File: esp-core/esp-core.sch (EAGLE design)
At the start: 6 parts

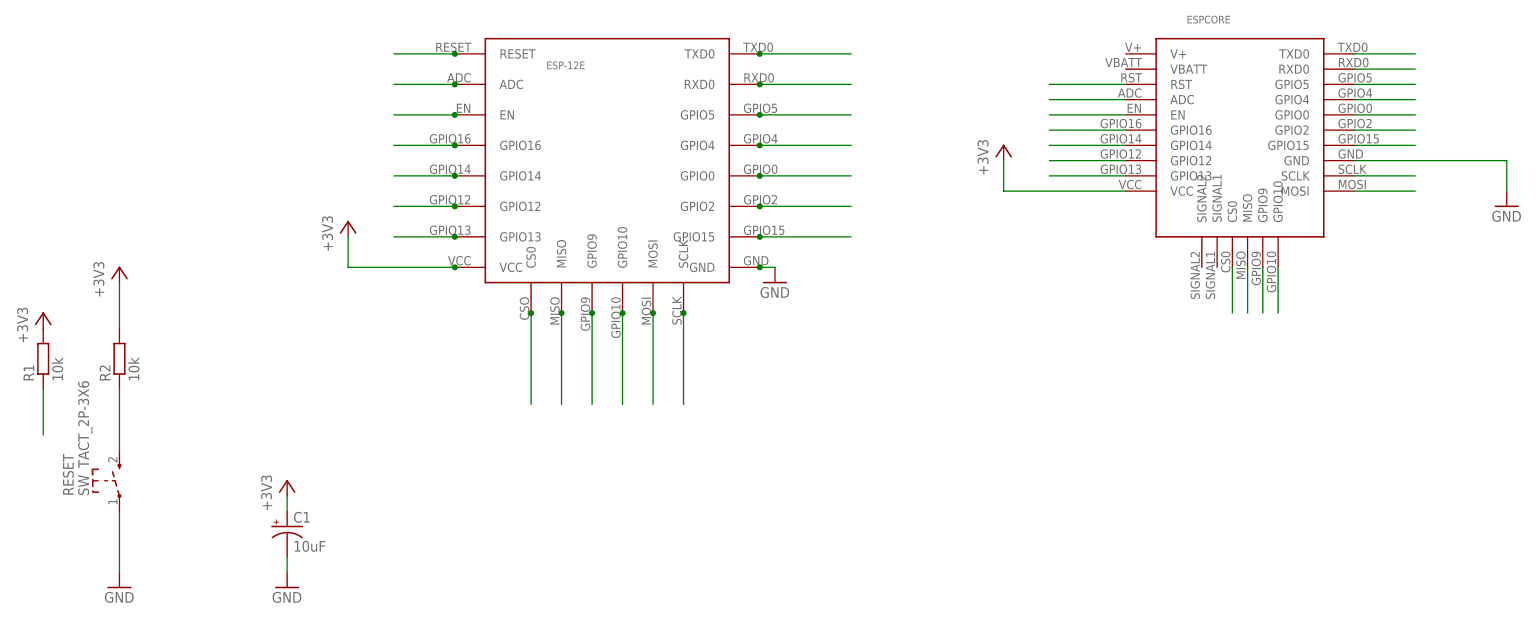
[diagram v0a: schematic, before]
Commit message: Add pull-up and down resistors to 'special' pins - GPIO0 and GPIO15
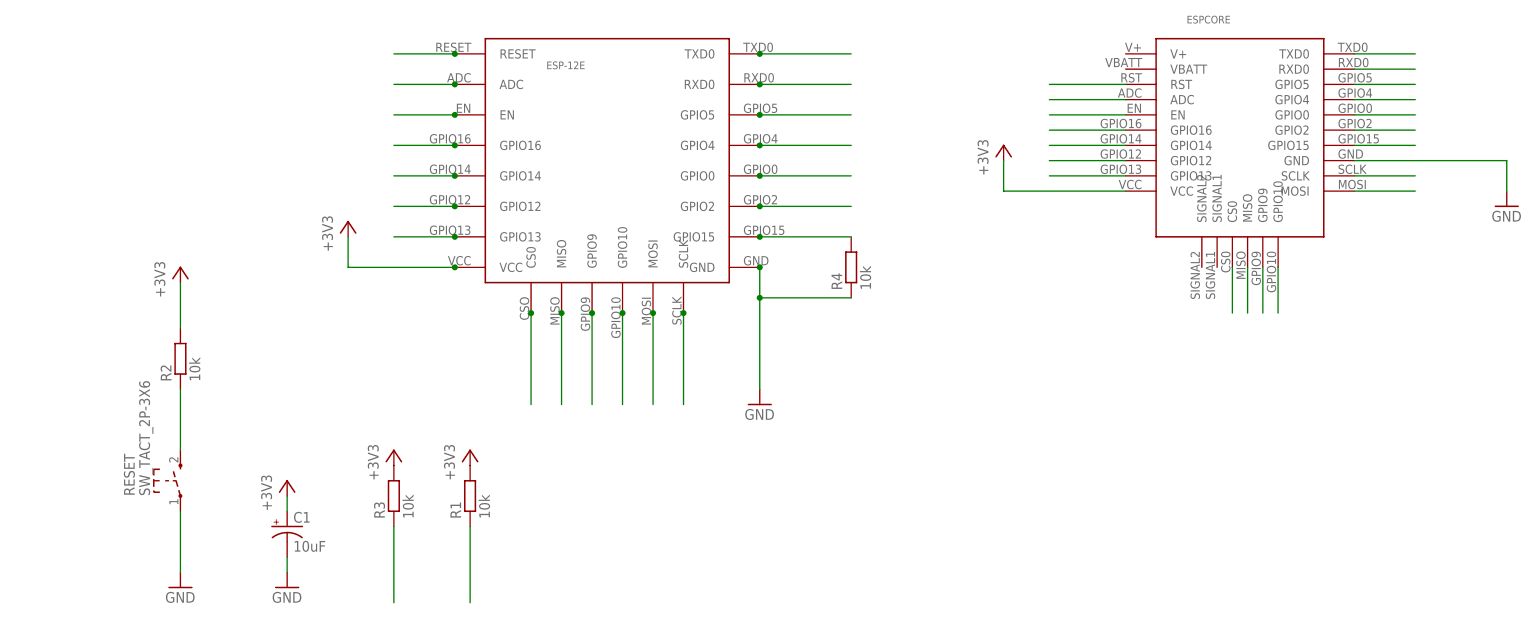
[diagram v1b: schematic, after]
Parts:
- added R3, R4: 10k, dp_devices:RESISTOR-1206
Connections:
- net +3V3: now also R3.2
- net GND: now also R4.1
- net GPIO0: now also R3.1
- net GPIO15: now also R4.2
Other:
- moved on the sheet: R1, R2, RESET
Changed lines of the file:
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@@
 <part name="ESPCORE" library="ESPstack" deviceset="ESP-BOARD" device=""/>
 <part name="ESP-12E" library="ESPstack" deviceset="ESP-12E" device=""/>
+<part name="R3" library="dp_devices" deviceset="RESISTOR" device="-1206" value="10k"/>
+<part name="R4" library="dp_devices" deviceset="RESISTOR" device="-1206" value="10k"/>
+<part name="+3V6" library="supply1" deviceset="+3V3" device=""/>
 </parts>
 <sheets>
@@
 </plain>
 <instances>
-<instance part="R1" gate="G$1" x="-144.78" y="-10.16" rot="R90"/>
-<instance part="R2" gate="G$1" x="-132.08" y="-10.16" rot="R90"/>
-<instance part="RESET" gate="SW" x="-132.08" y="-30.48" rot="R90"/>
+<instance part="R1" gate="G$1" x="-73.66" y="-33.02" rot="R90"/>
+<instance part="R2" gate="G$1" x="-121.92" y="-10.16" rot="R90"/>
+<instance part="RESET" gate="SW" x="-121.92" y="-30.48" rot="R90"/>
 <instance part="+3V1" gate="G$1" x="15.24" y="25.4"/>
-<instance part="+3V2" gate="G$1" x="-144.78" y="-2.54"/>
-<instance part="+3V3" gate="G$1" x="-132.08" y="5.08"/>
+<instance part="+3V2" gate="G$1" x="-73.66" y="-25.4"/>
+<instance part="+3V3" gate="G$1" x="-121.92" y="5.08"/>
 <instance part="+3V4" gate="G$1" x="-93.98" y="12.7"/>
 <instance part="GND1" gate="1" x="99.06" y="15.24"/>
-<instance part="GND3" gate="1" x="-22.86" y="2.54"/>
-<instance part="GND4" gate="1" x="-132.08" y="-48.26"/>
+<instance part="GND3" gate="1" x="-25.4" y="-17.78"/>
+<instance part="GND4" gate="1" x="-121.92" y="-48.26"/>
 <instance part="+3V5" gate="G$1" x="-104.14" y="-30.48"/>
 <instance part="GND5" gate="1" x="-104.14" y="-48.26"/>
@@
 <instance part="ESPCORE" gate="G$1" x="53.34" y="27.94"/>
 <instance part="ESP-12E" gate="G$1" x="-48.26" y="17.78"/>
+<instance part="R3" gate="G$1" x="-86.36" y="-33.02" rot="R90"/>
+<instance part="R4" gate="G$1" x="-10.16" y="5.08" rot="R90"/>
+<instance part="+3V6" gate="G$1" x="-86.36" y="-25.4"/>
 </instances>
 <busses>
@@
 <wire x1="73.66" y1="30.48" x2="83.82" y2="30.48" width="0.1524" layer="91"/>
 </segment>
+<segment>
+<pinref part="R3" gate="G$1" pin="1"/>
+<wire x1="-86.36" y1="-38.1" x2="-86.36" y2="-50.8" width="0.1524" layer="91"/>
+</segment>
 </net>
 <net name="GPIO2" class="0">
@@
 <pinref part="ESP-12E" gate="G$1" pin="GPIO15"/>
 <junction x="-25.4" y="10.16"/>
+<pinref part="R4" gate="G$1" pin="2"/>
 </segment>
 <segment>
@@
 <pinref part="GND4" gate="1" pin="GND"/>
 <pinref part="RESET" gate="SW" pin="1"/>
-<wire x1="-132.08" y1="-35.56" x2="-132.08" y2="-45.72" width="0.1524" layer="91"/>
-</segment>
-<segment>
-<wire x1="-25.4" y1="5.08" x2="-22.86" y2="5.08" width="0.1524" layer="91"/>
+<wire x1="-121.92" y1="-35.56" x2="-121.92" y2="-45.72" width="0.1524" layer="91"/>
+</segment>
+<segment>
+<wire x1="-25.4" y1="5.08" x2="-25.4" y2="0" width="0.1524" layer="91"/>
 <pinref part="GND3" gate="1" pin="GND"/>
 <pinref part="ESP-12E" gate="G$1" pin="GND"/>
 <junction x="-25.4" y="5.08"/>
+<pinref part="R4" gate="G$1" pin="1"/>
+<wire x1="-25.4" y1="0" x2="-25.4" y2="-15.24" width="0.1524" layer="91"/>
+<wire x1="-10.16" y1="0" x2="-25.4" y2="0" width="0.1524" layer="91"/>
+<junction x="-25.4" y="0"/>
 </segment>
 <segment>
@@
 <pinref part="+3V3" gate="G$1" pin="+3V3"/>
 <pinref part="R2" gate="G$1" pin="2"/>
-<wire x1="-132.08" y1="2.54" x2="-132.08" y2="-5.08" width="0.1524" layer="91"/>
+<wire x1="-121.92" y1="2.54" x2="-121.92" y2="-5.08" width="0.1524" layer="91"/>
 </segment>
 <segment>
@@
 <wire x1="-104.14" y1="-35.56" x2="-104.14" y2="-33.02" width="0.1524" layer="91"/>
 </segment>
+<segment>
+<pinref part="R3" gate="G$1" pin="2"/>
+<pinref part="+3V6" gate="G$1" pin="+3V3"/>
+</segment>
 </net>
 <net name="RESET" class="0">
@@
 <pinref part="RESET" gate="SW" pin="3"/>
 <pinref part="R2" gate="G$1" pin="1"/>
-<wire x1="-132.08" y1="-25.4" x2="-132.08" y2="-15.24" width="0.1524" layer="91"/>
+<wire x1="-121.92" y1="-25.4" x2="-121.92" y2="-15.24" width="0.1524" layer="91"/>
 </segment>
 <segment>
@@
 <segment>
 <pinref part="R1" gate="G$1" pin="1"/>
-<wire x1="-144.78" y1="-22.86" x2="-144.78" y2="-15.24" width="0.1524" layer="91"/>
-</segment>
-<segment>
+<wire x1="-73.66" y1="-50.8" x2="-73.66" y2="-38.1" width="0.1524" layer="91"/>
+</segment>
+<segment>

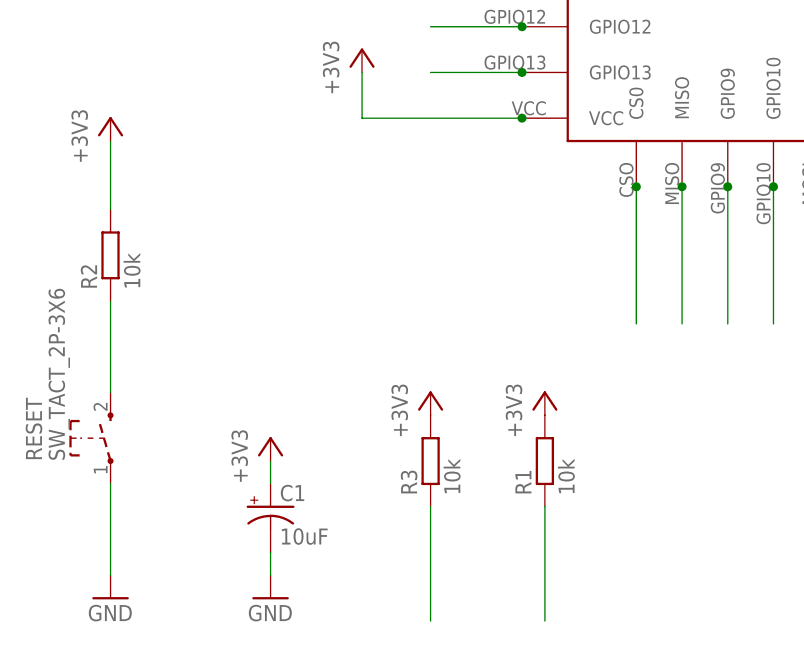
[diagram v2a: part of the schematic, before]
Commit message: Fix button on board
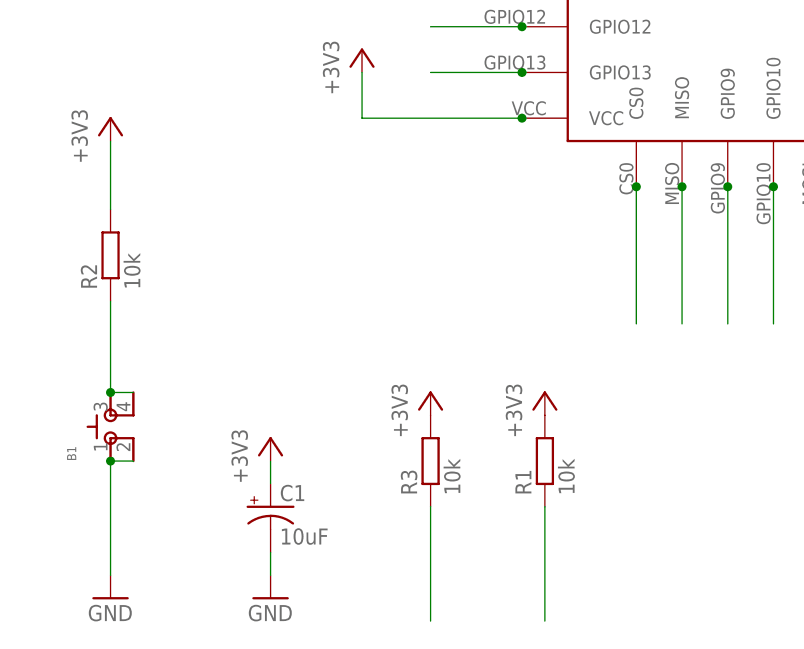
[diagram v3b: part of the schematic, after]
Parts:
- removed RESET: SW_TACT_2P-3X6, dp_devices:SW_TACT_2P-3X6
- added B1: (no value), ESPstack:SKSCLDE010
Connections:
- net GND: now also B1.1, B1.2; no longer RESET.1
- net RESET: now also B1.3, B1.4; no longer RESET.3
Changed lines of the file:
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@@
 <part name="R1" library="dp_devices" deviceset="RESISTOR" device="-1206" value="10k"/>
 <part name="R2" library="dp_devices" deviceset="RESISTOR" device="-1206" value="10k"/>
-<part name="RESET" library="dp_devices" deviceset="SW_TACT_2P" device="-3X6"/>
 <part name="+3V1" library="supply1" deviceset="+3V3" device=""/>
 <part name="+3V2" library="supply1" deviceset="+3V3" device=""/>
@@
 <part name="R4" library="dp_devices" deviceset="RESISTOR" device="-1206" value="10k"/>
 <part name="+3V6" library="supply1" deviceset="+3V3" device=""/>
+<part name="B1" library="ESPstack" deviceset="SKSCLDE010" device=""/>
 </parts>
 <sheets>
@@
 <instance part="R1" gate="G$1" x="-73.66" y="-33.02" rot="R90"/>
 <instance part="R2" gate="G$1" x="-121.92" y="-10.16" rot="R90"/>
-<instance part="RESET" gate="SW" x="-121.92" y="-30.48" rot="R90"/>
 <instance part="+3V1" gate="G$1" x="15.24" y="25.4"/>
 <instance part="+3V2" gate="G$1" x="-73.66" y="-25.4"/>
@@
 <instance part="R4" gate="G$1" x="-10.16" y="5.08" rot="R90"/>
 <instance part="+3V6" gate="G$1" x="-86.36" y="-25.4"/>
+<instance part="B1" gate="G$1" x="-121.92" y="-27.94" rot="R90"/>
 </instances>
 <busses>
@@
 <segment>
 <pinref part="GND4" gate="1" pin="GND"/>
-<pinref part="RESET" gate="SW" pin="1"/>
-<wire x1="-121.92" y1="-35.56" x2="-121.92" y2="-45.72" width="0.1524" layer="91"/>
+<wire x1="-121.92" y1="-33.02" x2="-121.92" y2="-45.72" width="0.1524" layer="91"/>
+<pinref part="B1" gate="G$1" pin="1"/>
+<pinref part="B1" gate="G$1" pin="2"/>
+<wire x1="-121.92" y1="-33.02" x2="-119.38" y2="-33.02" width="0.1524" layer="91"/>
+<junction x="-121.92" y="-33.02"/>
 </segment>
 <segment>
@@
 <net name="RESET" class="0">
 <segment>
-<pinref part="RESET" gate="SW" pin="3"/>
 <pinref part="R2" gate="G$1" pin="1"/>
 <wire x1="-121.92" y1="-25.4" x2="-121.92" y2="-15.24" width="0.1524" layer="91"/>
-</segment>
-<segment>
+<pinref part="B1" gate="G$1" pin="4"/>
+<pinref part="B1" gate="G$1" pin="3"/>
+<wire x1="-119.38" y1="-25.4" x2="-121.92" y2="-25.4" width="0.1524" layer="91"/>
+<junction x="-121.92" y="-25.4"/>
+</segment>
+<segment>

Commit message: core board fixes
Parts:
- renumbered B1 to RESET
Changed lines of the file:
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@@
 <part name="R4" library="dp_devices" deviceset="RESISTOR" device="-1206" value="10k"/>
 <part name="+3V6" library="supply1" deviceset="+3V3" device=""/>
-<part name="B1" library="ESPstack" deviceset="SKSCLDE010" device=""/>
+<part name="RESET" library="ESPstack" deviceset="SKSCLDE010" device=""/>
 </parts>
 <sheets>
@@
 <instance part="R4" gate="G$1" x="-10.16" y="5.08" rot="R90"/>
 <instance part="+3V6" gate="G$1" x="-86.36" y="-25.4"/>
-<instance part="B1" gate="G$1" x="-121.92" y="-27.94" rot="R90"/>
+<instance part="RESET" gate="G$1" x="-121.92" y="-27.94" rot="R90"/>
 </instances>
 <busses>
@@
 <pinref part="GND4" gate="1" pin="GND"/>
 <wire x1="-121.92" y1="-33.02" x2="-121.92" y2="-45.72" width="0.1524" layer="91"/>
-<pinref part="B1" gate="G$1" pin="1"/>
-<pinref part="B1" gate="G$1" pin="2"/>
+<pinref part="RESET" gate="G$1" pin="1"/>
+<pinref part="RESET" gate="G$1" pin="2"/>
 <wire x1="-121.92" y1="-33.02" x2="-119.38" y2="-33.02" width="0.1524" layer="91"/>
 <junction x="-121.92" y="-33.02"/>
@@
 <pinref part="R2" gate="G$1" pin="1"/>
 <wire x1="-121.92" y1="-25.4" x2="-121.92" y2="-15.24" width="0.1524" layer="91"/>
-<pinref part="B1" gate="G$1" pin="4"/>
-<pinref part="B1" gate="G$1" pin="3"/>
+<pinref part="RESET" gate="G$1" pin="4"/>
+<pinref part="RESET" gate="G$1" pin="3"/>
 <wire x1="-119.38" y1="-25.4" x2="-121.92" y2="-25.4" width="0.1524" layer="91"/>
 <junction x="-121.92" y="-25.4"/>

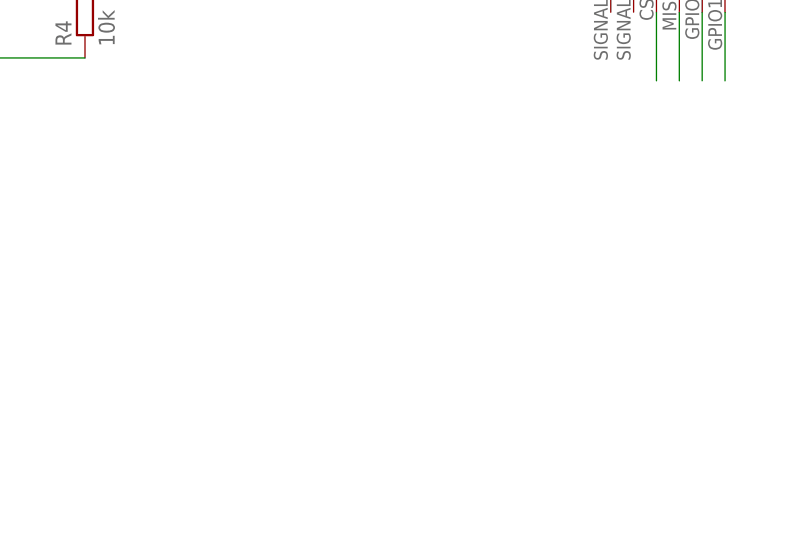
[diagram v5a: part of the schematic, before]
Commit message: Unify all boards, buttons in the same place, board dimension reduced to 1.32inch
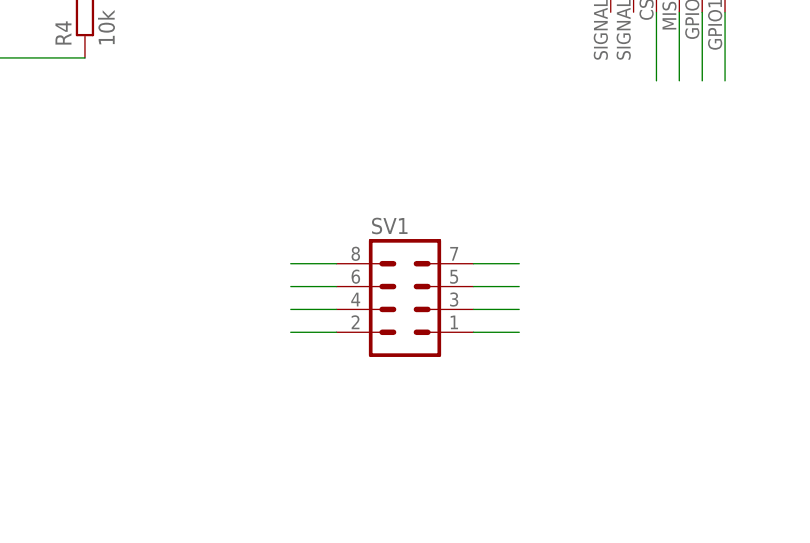
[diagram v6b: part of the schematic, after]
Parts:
- added SV1: (no value), con-lstb:MA04-2
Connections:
- net +3V3: now also SV1.7
- net EN: now also SV1.3
- net GND: now also SV1.2
- net GPIO0: now also SV1.6
- net GPIO2: now also SV1.4
- net RESET: now also SV1.5
- net RXD0: now also SV1.8
- net TXD0: now also SV1.1
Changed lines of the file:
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@@
 <part name="+3V6" library="supply1" deviceset="+3V3" device=""/>
 <part name="RESET" library="ESPstack" deviceset="SKSCLDE010" device=""/>
+<part name="SV1" library="con-lstb" deviceset="MA04-2" device=""/>
 </parts>
 <sheets>
@@
 <instance part="+3V6" gate="G$1" x="-86.36" y="-25.4"/>
 <instance part="RESET" gate="G$1" x="-121.92" y="-27.94" rot="R90"/>
+<instance part="SV1" gate="G$1" x="25.4" y="-25.4"/>
 </instances>
 <busses>
@@
 <wire x1="73.66" y1="40.64" x2="83.82" y2="40.64" width="0.1524" layer="91"/>
 </segment>
+<segment>
+<pinref part="SV1" gate="G$1" pin="1"/>
+<wire x1="33.02" y1="-30.48" x2="38.1" y2="-30.48" width="0.1524" layer="91"/>
+</segment>
 </net>
 <net name="RXD0" class="0">
@@
 <wire x1="73.66" y1="38.1" x2="83.82" y2="38.1" width="0.1524" layer="91"/>
 </segment>
+<segment>
+<pinref part="SV1" gate="G$1" pin="8"/>
+<wire x1="17.78" y1="-22.86" x2="12.7" y2="-22.86" width="0.1524" layer="91"/>
+</segment>
 </net>
 <net name="GPIO5" class="0">
@@
 <wire x1="-86.36" y1="-38.1" x2="-86.36" y2="-50.8" width="0.1524" layer="91"/>
 </segment>
+<segment>
+<pinref part="SV1" gate="G$1" pin="6"/>
+<wire x1="17.78" y1="-25.4" x2="12.7" y2="-25.4" width="0.1524" layer="91"/>
+</segment>
 </net>
 <net name="GPIO2" class="0">
@@
 <pinref part="ESPCORE" gate="G$1" pin="GPIO2"/>
 <wire x1="73.66" y1="27.94" x2="83.82" y2="27.94" width="0.1524" layer="91"/>
+</segment>
+<segment>
+<pinref part="SV1" gate="G$1" pin="4"/>
+<wire x1="17.78" y1="-27.94" x2="12.7" y2="-27.94" width="0.1524" layer="91"/>
 </segment>
 </net>
@@
 <wire x1="-104.14" y1="-43.18" x2="-104.14" y2="-45.72" width="0.1524" layer="91"/>
 </segment>
+<segment>
+<pinref part="SV1" gate="G$1" pin="2"/>
+<wire x1="17.78" y1="-30.48" x2="12.7" y2="-30.48" width="0.1524" layer="91"/>
+</segment>
 </net>
 <net name="+3V3" class="0">
@@
 <pinref part="R3" gate="G$1" pin="2"/>
 <pinref part="+3V6" gate="G$1" pin="+3V3"/>
+</segment>
+<segment>
+<pinref part="SV1" gate="G$1" pin="7"/>
+<wire x1="33.02" y1="-22.86" x2="38.1" y2="-22.86" width="0.1524" layer="91"/>
 </segment>
 </net>
@@
 <wire x1="35.56" y1="35.56" x2="22.86" y2="35.56" width="0.1524" layer="91"/>
 </segment>
+<segment>
+<pinref part="SV1" gate="G$1" pin="5"/>
+<wire x1="33.02" y1="-25.4" x2="38.1" y2="-25.4" width="0.1524" layer="91"/>
+</segment>
 </net>
 <net name="EN" class="0">
@@
 <wire x1="35.56" y1="30.48" x2="22.86" y2="30.48" width="0.1524" layer="91"/>
 </segment>
-</net>
+<segment>
+<pinref part="SV1" gate="G$1" pin="3"/>
+<wire x1="33.02" y1="-27.94" x2="38.1" y2="-27.94" width="0.1524" layer="91"/>
+</segment>
+</net>
